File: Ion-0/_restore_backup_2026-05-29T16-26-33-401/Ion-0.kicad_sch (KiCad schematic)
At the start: 16 parts, among them J1 Beaglebone-green-P9, J2 Beaglebone-green-P8, J3 Conn_02x06_Odd_Even, J4 Conn_02x06_Odd_Even, J5 Conn_02x06_Odd_Even

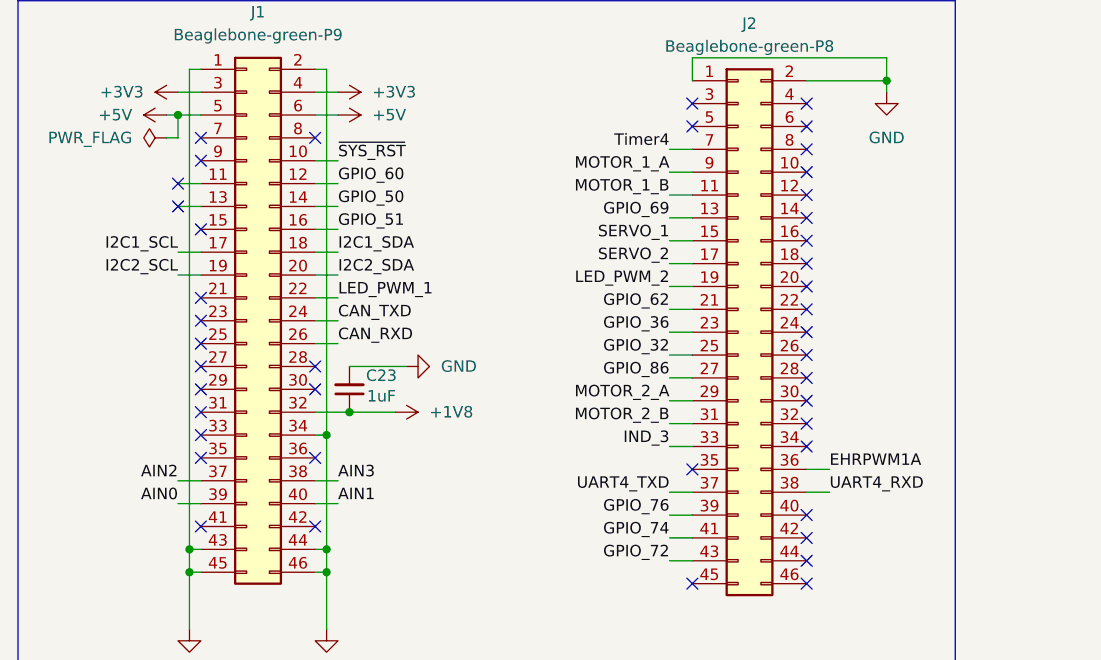
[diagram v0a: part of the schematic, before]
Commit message: finished tracing, need to fix m3 holes, text, impedance match antenna, via stiching
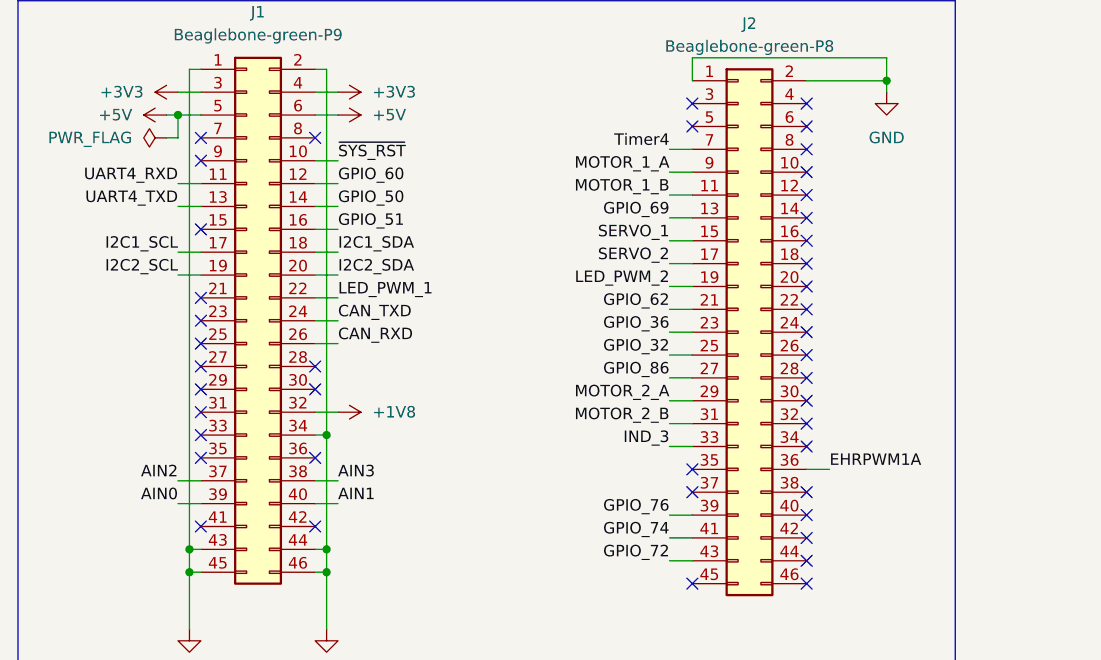
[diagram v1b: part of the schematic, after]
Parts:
- removed C23: 1uF, Capacitor_SMD:C_0603_1608Metric, symbol Device:C_Small
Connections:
- net UART4_RXD: now also J1.11 (Pin_11); no longer J2.38 (Pin_38)
- net UART4_TXD: now also J1.13 (Pin_13); no longer J2.37 (Pin_37)
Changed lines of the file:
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@@
 	)
 	(junction
-		(at 52.07 60.96)
-		(diameter 0)
-		(color 0 0 0 0)
-	)
-	(junction
 		(at 74.93 163.83)
 		(diameter 0)
@@
 	)
 	(no_connect
-		(at 33.02 35.56)
+		(at 102.87 69.85)
 	)
 	(no_connect
@@
 	)
 	(no_connect
-		(at 33.02 38.1)
-	)
-	(no_connect
 		(at 102.87 34.29)
 	)
@@
 	)
 	(no_connect
+		(at 90.17 69.85)
+	)
+	(no_connect
 		(at 102.87 46.99)
 	)
@@
 	(wire
 		(pts
-			(xy 102.87 69.85) (xy 105.41 69.85)
-		)
-		(stroke
-			(width 0)
-			(type default)
-		)
-	)
-	(wire
-		(pts
-			(xy 52.07 60.96) (xy 57.15 60.96)
-		)
-		(stroke
-			(width 0)
-			(type default)
-		)
-	)
-	(wire
-		(pts
 			(xy 179.07 59.69) (xy 179.07 50.8)
 		)
@@
 	(wire
 		(pts
-			(xy 87.63 69.85) (xy 90.17 69.85)
-		)
-		(stroke
-			(width 0)
-			(type default)
-		)
-	)
-	(wire
-		(pts
 			(xy 139.7 161.29) (xy 142.24 161.29)
 		)
@@
 	(wire
 		(pts
-			(xy 52.07 55.88) (xy 58.42 55.88)
-		)
-		(stroke
-			(width 0)
-			(type default)
-		)
-	)
-	(wire
-		(pts
 			(xy 142.24 168.91) (xy 135.89 168.91)
 		)
@@
 	(wire
 		(pts
-			(xy 48.26 60.96) (xy 52.07 60.96)
+			(xy 48.26 60.96) (xy 50.8 60.96)
 		)
 		(stroke
@@
 	)
 	(label "UART4_RXD"
-		(at 105.41 69.85 0)
+		(at 33.02 35.56 180)
 		(effects
 			(font
 				(size 1.27 1.27)
 			)
-			(justify left bottom)
+			(justify right bottom)
 		)
 	)
@@
 	)
 	(label "UART4_TXD"
-		(at 87.63 69.85 180)
+		(at 33.02 38.1 180)
 		(effects
 			(font
@@
 	)
 	(symbol
-		(lib_id "Device:C_Small")
-		(at 52.07 58.42 180)
-		(unit 1)
-		(body_style 1)
-		(exclude_from_sim no)
-		(in_bom yes)
-		(on_board yes)
-		(in_pos_files yes)
-		(dnp no)
-		(property "Reference" "C23"
-			(at 55.626 56.896 0)
-			(show_name no)
-			(do_not_autoplace no)
-			(effects
-				(font
-					(size 1.27 1.27)
-				)
-			)
-		)
-		(property "Value" "1uF"
-			(at 55.626 59.182 0)
-			(show_name no)
-			(do_not_autoplace no)
-			(effects
-				(font
-					(size 1.27 1.27)
-				)
-			)
-		)
-		(property "Footprint" "Capacitor_SMD:C_0603_1608Metric"
-			(at 52.07 58.42 0)
-			(hide yes)
-			(show_name no)
-			(do_not_autoplace no)
-			(effects
-				(font
-					(size 1.27 1.27)
-				)
-			)
-		)
-		(property "Datasheet" ""
-			(at 52.07 58.42 0)
-			(hide yes)
-			(show_name no)
-			(do_not_autoplace no)
-			(effects
-				(font
-					(size 1.27 1.27)
-				)
-			)
-		)
-		(property "Description" "Unpolarized capacitor, small symbol"
-			(at 52.07 58.42 0)
-			(hide yes)
-			(show_name no)
-			(do_not_autoplace no)
-			(effects
-				(font
-					(size 1.27 1.27)
-				)
-			)
-		)
-		(pin "2"
-		)
-		(pin "1"
-		)
-		(instances
-			(project "Ion-0"
-				(path "/8323d88f-a402-4af7-9e3a-bb7cf2dffd76"
-					(reference "C23")
-					(unit 1)
-				)
-			)
-		)
-	)
-	(symbol
 		(lib_id "power:GND")
 		(at 34.29 85.09 0)
@@
 	(symbol
 		(lib_id "power:+1V8")
-		(at 57.15 60.96 270)
+		(at 50.8 60.96 270)
 		(unit 1)
 		(body_style 1)
@@
 		(fields_autoplaced yes)
 		(property "Reference" "#PWR05"
-			(at 53.34 60.96 0)
+			(at 46.99 60.96 0)
 			(hide yes)
 			(show_name no)
@@
 		)
 		(property "Value" "+1V8"
-			(at 60.96 60.9599 90)
+			(at 54.61 60.9599 90)
 			(show_name no)
 			(do_not_autoplace no)
@@
 		)
 		(property "Footprint" ""
-			(at 57.15 60.96 0)
+			(at 50.8 60.96 0)
 			(hide yes)
 			(show_name no)
@@
 		)
 		(property "Datasheet" ""
-			(at 57.15 60.96 0)
+			(at 50.8 60.96 0)
 			(hide yes)
 			(show_name no)
@@
 		)
 		(property "Description" "Power symbol creates a global label with name \"+1V8\""
-			(at 57.15 60.96 0)
+			(at 50.8 60.96 0)
 			(hide yes)
 			(show_name no)
@@
 					(unit 1)
 				)
-			)
-		)
-	)
-	(symbol
-		(lib_id "power:GND")
-		(at 58.42 55.88 90)
-		(unit 1)
-		(body_style 1)
-		(exclude_from_sim no)
-		(in_bom yes)
-		(on_board yes)
-		(in_pos_files yes)
-		(dnp no)
-		(fields_autoplaced yes)
-		(property "Reference" "#PWR085"
-			(at 64.77 55.88 0)
-			(hide yes)
-			(show_name no)
-			(do_not_autoplace no)
-			(effects
-				(font
-					(size 1.27 1.27)
-				)
-			)
-		)
-		(property "Value" "GND"
-			(at 62.23 55.8799 90)
-			(show_name no)
-			(do_not_autoplace no)
-			(effects
-				(font
-					(size 1.27 1.27)
-				)
-				(justify right)
-			)
-		)
-		(property "Footprint" ""
-			(at 58.42 55.88 0)
-			(hide yes)
-			(show_name no)
-			(do_not_autoplace no)
-			(effects
-				(font
-					(size 1.27 1.27)
-				)
-			)
-		)
-		(property "Datasheet" ""
-			(at 58.42 55.88 0)
-			(hide yes)
-			(show_name no)
-			(do_not_autoplace no)
-			(effects
-				(font
-					(size 1.27 1.27)
-				)
-			)
-		)
-		(property "Description" "Power symbol creates a global label with name \"GND\" , ground"
-			(at 58.42 55.88 0)
-			(hide yes)
-			(show_name no)
-			(do_not_autoplace no)
-			(effects
-				(font
-					(size 1.27 1.27)
-				)
-			)
-		)
-		(pin "1"
-		)
-		(instances
-			(project "Ion-0"
-				(path "/8323d88f-a402-4af7-9e3a-bb7cf2dffd76"
-					(reference "#PWR085")
-					(unit 1)
-				)
